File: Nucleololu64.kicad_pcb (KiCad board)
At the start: 2 copper layers, 70 x 80 mm, 82 parts, among them CN1 CONN_02X19, CN2 CONN_02X19, J2 CONN_01X06, J3 CONN_02X06, J4 CONN_01X03, P11 KK-2.54-4W, P12 KK-2.54-4W, P2 KK-2.54-4W, P3 KK-2.54-4W, P4 CONN_02X02, P5 KK-2.54-4W, P6 KK-2.54-4W, P7 KK-2.54-4W, P8 KK-2.54-4W, Q1 IRLB8743PBF, Q2 IRLB8743PBF, Q3 IRLB8743PBF, U1 TPS5420, U2 Pololu, U3 Pololu, U4 Pololu, U5 Pololu

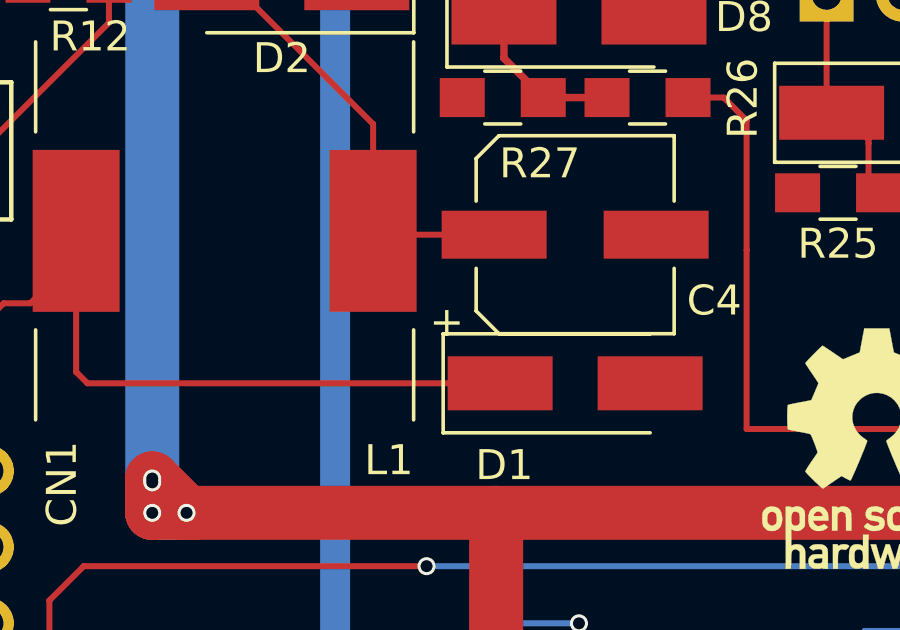
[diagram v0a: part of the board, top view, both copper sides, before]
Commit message: added many manf#
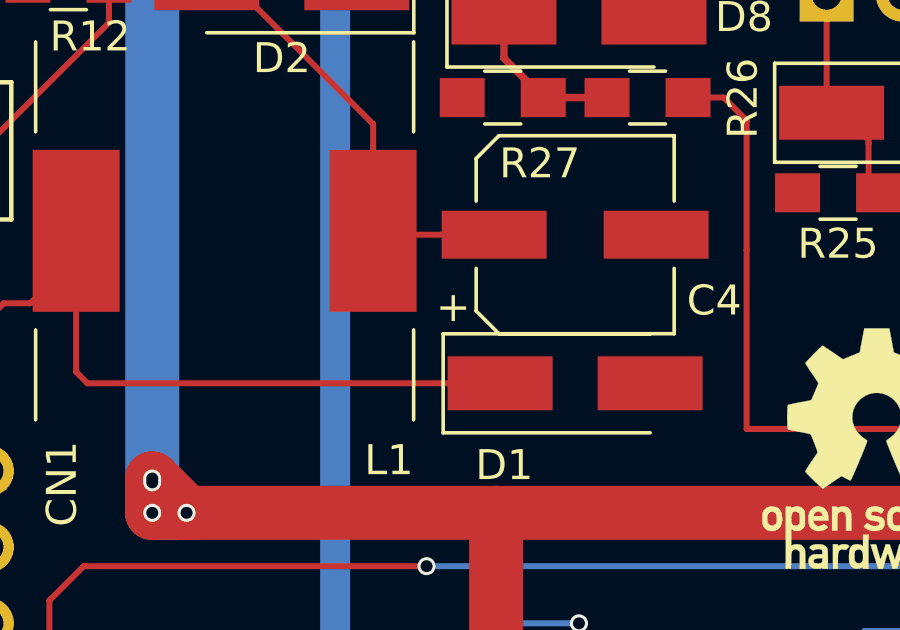
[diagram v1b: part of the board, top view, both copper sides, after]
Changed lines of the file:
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@@
       (effects (font (size 1 1) (thickness 0.15)))
     )
-    (fp_text user + (at -4.28 2.91) (layer F.SilkS)
+    (fp_text user + (at -4.064 2.413) (layer F.SilkS)
       (effects (font (size 1 1) (thickness 0.15)))
     )
